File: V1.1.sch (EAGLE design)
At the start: 28 parts, among them U1 AP63205WU-7SOIC_05WU-7_DIO-M, U3 ATTINY828-AU32A_ATM-M

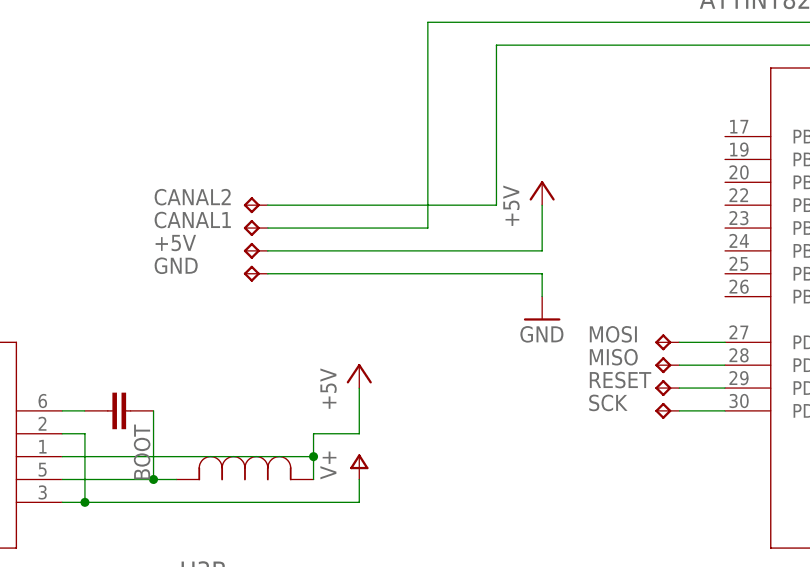
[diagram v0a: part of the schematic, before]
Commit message: V1.2
El esquemático es el mismo, la placa tiene mejores tolerancias, mejor distribución nuevos pads para señales y cumple con las especificaciones de jlcpcb
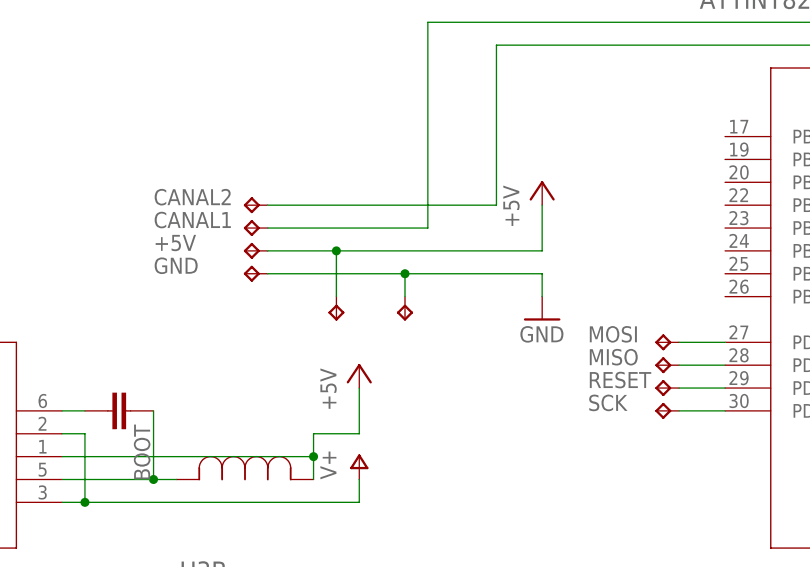
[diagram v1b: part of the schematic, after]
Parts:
- added TP5, TP9: TPTP13SQ, testpad:TPTP13SQ
- GND, V+: value TPTP15SQ -> TPTP20SQ; device testpad:TPTP15SQ -> testpad:TPTP20SQ
- MISO, TP6, TP7, TP8: value TPTP06SQ -> TPTP12R; device testpad:TPTP06SQ -> testpad:TPTP12R
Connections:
- net +5V: now also TP9.TP
- net GND: now also TP5.TP

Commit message: Add files via upload
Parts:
- removed TP2: TPTP13SQ, testpad:TPTP13SQ
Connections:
- removed net CANAL2: TP2.TP, U3A.PA1
- removed net N$7: DRIVERMOTOR1.OUT2, MOTOR1.2
- removed net N$8: DRIVERMOTOR1.OUT1, MOTOR1.1
- net N$5: now also DRIVERMOTOR1.OUT2, MOTOR1.2
- net N$6: now also DRIVERMOTOR1.OUT1, MOTOR1.1
